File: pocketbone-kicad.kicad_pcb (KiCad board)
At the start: 2 copper layers, 55 x 35 mm, 64 parts, among them P1 USB_OTG, P2 USB_OTG, P3 CONN_01X10, P4 CONN_02X02, SW1 SW_PUSH_SMALL_H, SW2 SW_PUSH_SMALL_H, U1 SN74LVC1G07, U2 OSD3358, U3 24LC32AT-I/OT, U4 TPS2051C, Y2 24MHz

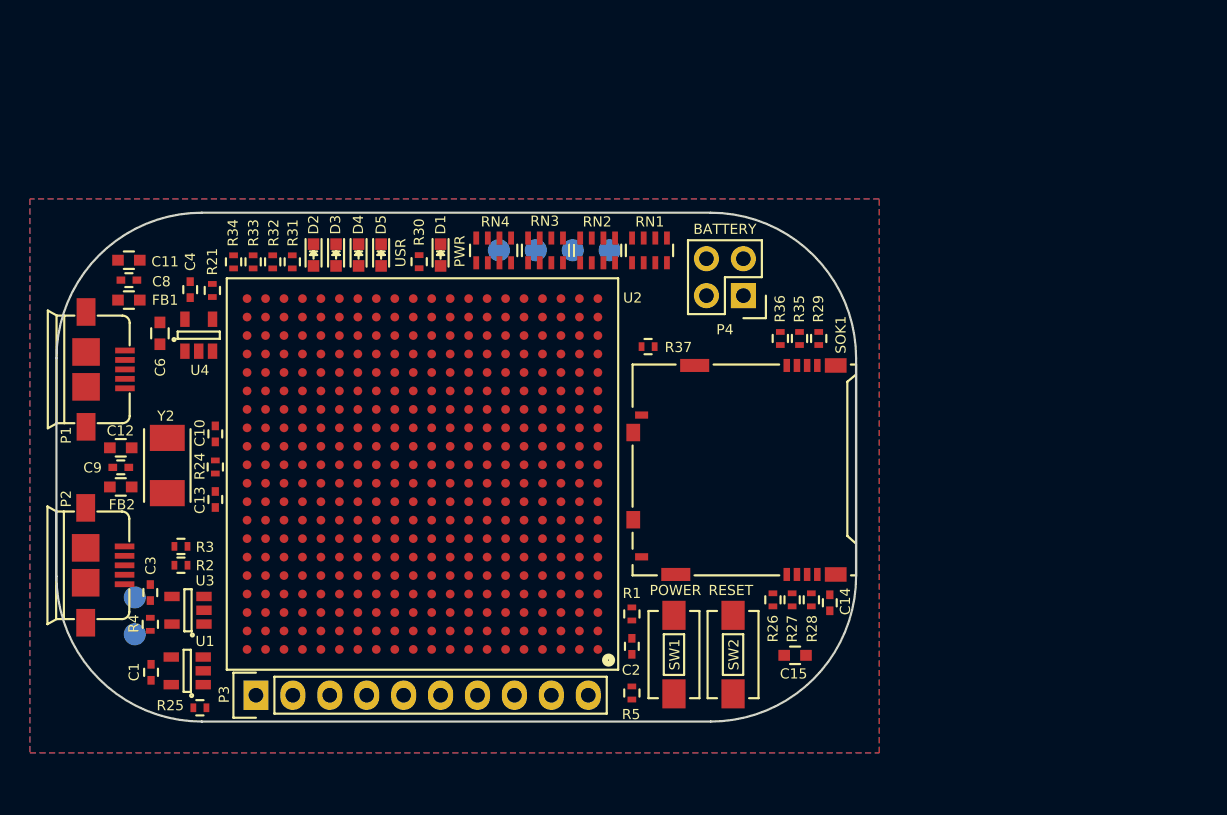
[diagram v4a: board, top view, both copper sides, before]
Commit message: Routing complete
Battery header updated in schmatic.
Plots and pictures updated.
Ready for design review.

Signed-off-by: Michael Welling <mwelling@ieee.org>
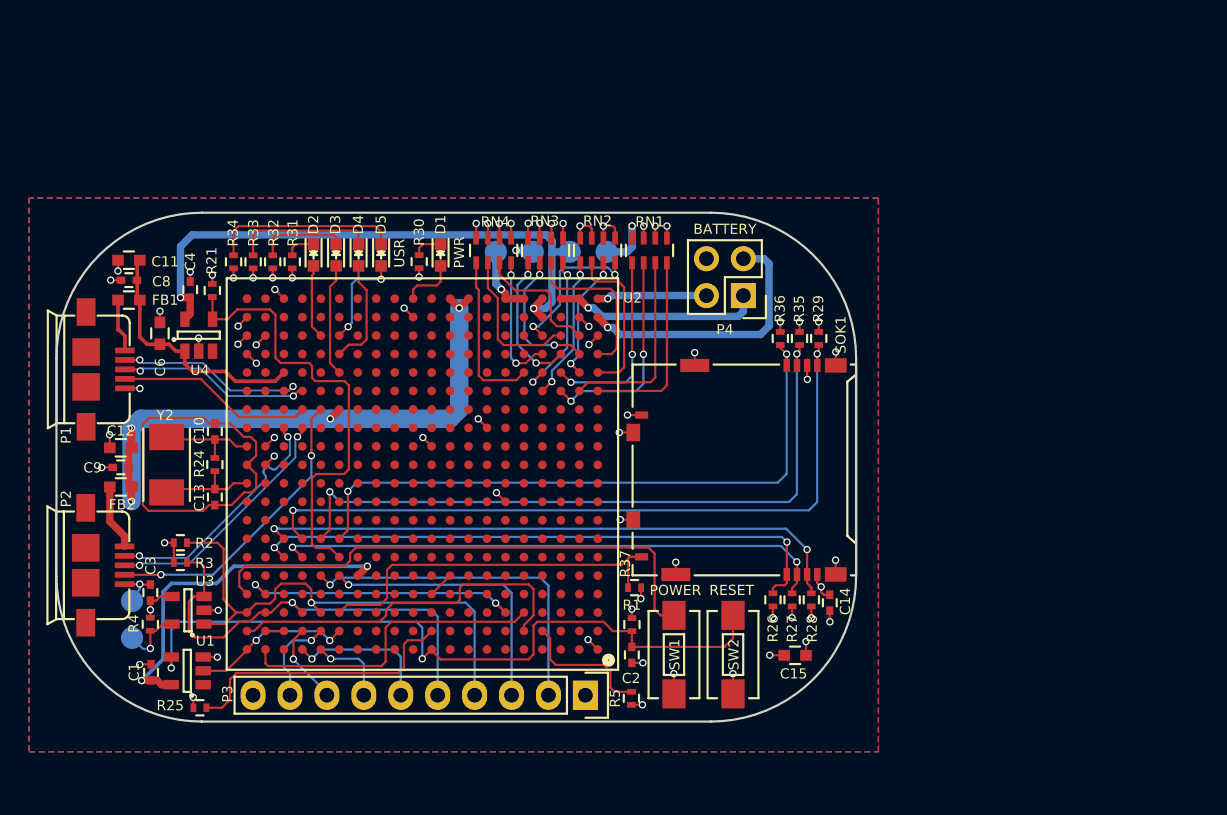
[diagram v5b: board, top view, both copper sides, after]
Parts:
- moved P3 22.7 mm to (142.3, 128.1), turned to 180 degrees
- moved R37 16.6 mm to (145.7, 120.7)
- moved G*** 1.79 mm to (113.1, 112.2)
- moved R2 1.55 mm to (114.5, 117.6)
- moved R3 1.11 mm to (114.5, 119.0)
- moved R1 0.73 mm to (145.5, 123.3)
- moved C2 0.59 mm to (145.5, 125.3)
- moved R5 0.37 mm to (145.5, 128.3)
- moved TP2 0.31 mm to (111.2, 124.2)
- moved TP3 0.31 mm to (111.2, 121.6)
- moved TP5 0.24 mm to (141.3, 97.6)
- moved TP6 0.24 mm to (143.8, 97.6)
- moved TP1 0.24 mm to (136.2, 97.6)
- moved TP4 0.24 mm to (138.7, 97.6)
- moved C13 0.17 mm to (116.9, 114.5)
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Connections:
- net Net-(P4-Pad3) renamed BAT_SENSE
- P4 pad 1: Net-(P4-Pad1) -> VBAT
- P4 pad 2: Net-(P4-Pad2) -> TS
- P4 pad 4: Net-(P4-Pad4) -> GND
- U2 pad W1: Net-(P4-Pad1) -> TS
- U2 pad Y2: Net-(P4-Pad2) -> VBAT
- U2 pad Y3: Net-(P4-Pad4) -> VBAT
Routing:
- net GND: track 0.00 -> 55.8 mm, vias 0 -> 57
- net Net-(C2-Pad1): track 0.00 -> 50.6 mm, vias 0 -> 2
- net MMC0_CLK: track 0.00 -> 50.2 mm, vias 0 -> 2
- net MMC0_DAT0: track 0.00 -> 47.2 mm, vias 0 -> 2
- net MMC0_DAT1: track 0.00 -> 44.0 mm, vias 0 -> 2
- net USB0_VBUS: track 0.00 -> 43.0 mm, vias 0 -> 4
- net MMC0_CMD: track 0.00 -> 41.3 mm, vias 0 -> 2
- net MMC0_DAT2: track 0.00 -> 40.9 mm, vias 0 -> 2
- net SYS_5V: track 0.00 -> 40.6 mm, vias 0 -> 2
- net MMC0_DAT3: track 0.00 -> 38.4 mm, vias 0 -> 2
- net Net-(SW1-Pad2): track 0.00 -> 36.8 mm
- net I2C0_SCL: track 0.00 -> 35.6 mm, vias 0 -> 1
- net I2C0_SDA: track 0.00 -> 31.7 mm, vias 0 -> 1
- net USB1_DRVVBUS: track 0.00 -> 30.9 mm
- net VDD_RTC: track 0.00 -> 27.0 mm, vias 0 -> 2
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- added copper zone on In1.Cu, net +3V3
- added copper zone on F.Cu, net GND
- added copper zone on In2.Cu, net GND
- removed copper zone on F.Cu, net +3V3
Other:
- copper layers 2 -> 4
- rule trace_min: 0.1524 -> 0.127
- board text added: "BS"
- board text added: "TS"
- board text added: "VBAT"

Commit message: Last minute tweaks
This version is posted to OSHpark site for anyone to order.
Order at your own risk.

Signed-off-by: Michael Welling <mwelling@ieee.org>
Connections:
- P1 pad 6: Net-(P1-Pad6) -> GND
- P1 pad 7: (no net) -> GND
- P1 pad 8: (no net) -> GND
- P1 pad 9: (no net) -> GND
- P2 pad 6: Net-(P2-Pad6) -> GND
- P2 pad 7: (no net) -> GND
- P2 pad 8: (no net) -> GND
- P2 pad 9: (no net) -> GND
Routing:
- net GND: track 55.8 -> 66.3 mm, vias 57 -> 65
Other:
- board text added: "PocketBone KiCAD Rev. 0 2017"

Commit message: Add OSHPark logo to the PCB and tweak the silk
OSHPark sponsoring the first proto run. \o/

https://oshpark.com/shared_projects/b7F6qftP

Signed-off-by: Michael Welling <mwelling@ieee.org>
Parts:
- added G***: LOGO, libs:oshpark, B.Cu at (135.6, 111.8)
- moved G*** 0.51 mm to (112.9, 111.8)
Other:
- board text added: "m_w"

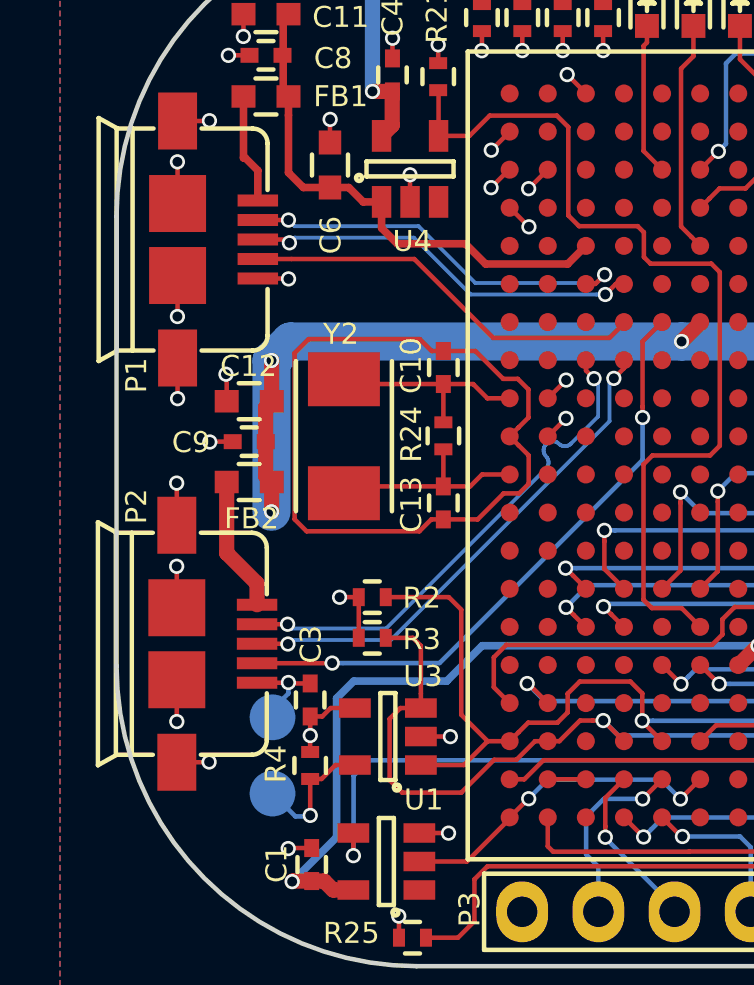
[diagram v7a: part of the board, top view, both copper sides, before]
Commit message: Updated Footprint and Schematic Librarys
The Paths of the USB and SOT Footprints pointed to local Directorys on
your HDD instead of the Project Folder
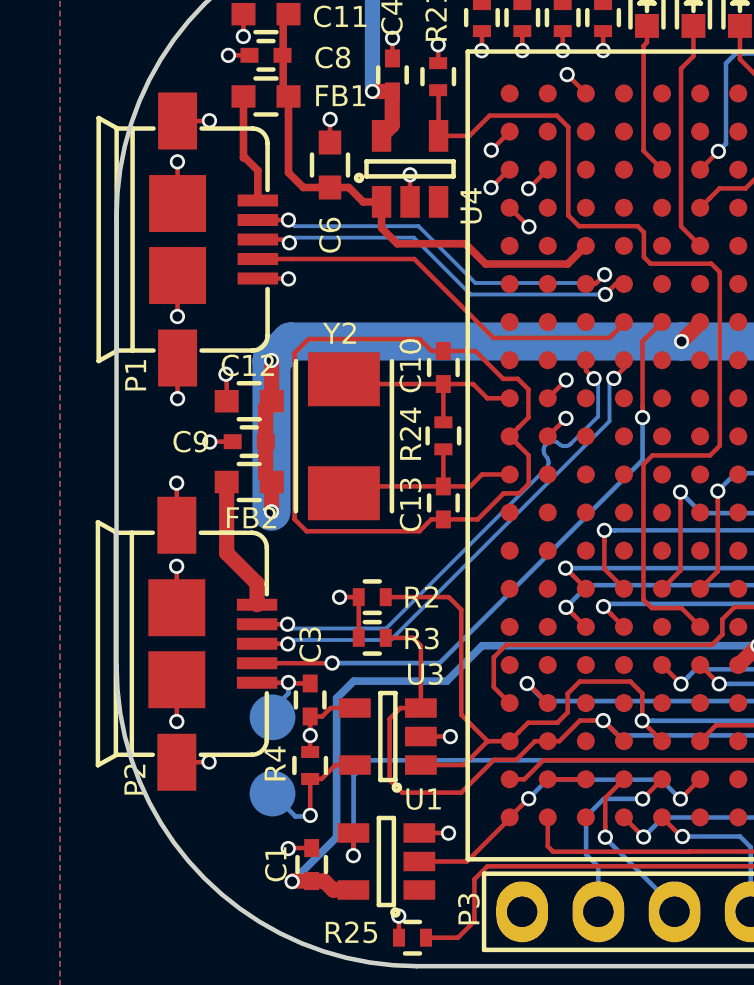
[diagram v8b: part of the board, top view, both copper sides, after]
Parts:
- P1, P2: footprint Sensors:USB_MICRO_B_ST-USB-001E -> pocketbone-kicad:USB_MICRO_B_ST-USB-001E
- U1, U3, U4: footprint SOT-23-5 -> pocketbone-kicad:SOT-23-5
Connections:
- P1 pad 7: GND -> (no net)
- P1 pad 8: GND -> (no net)
- P1 pad 9: GND -> (no net)
- P2 pad 7: GND -> (no net)
- P2 pad 8: GND -> (no net)
- P2 pad 9: GND -> (no net)
- U1 pad 1: Net-(U1-Pad1) -> (no net)
- U2 pad A11: Net-(U2-PadA11) -> (no net)
- U2 pad A12: Net-(U2-PadA12) -> (no net)
- U2 pad A13: Net-(U2-PadA13) -> (no net)
- U2 pad A14: Net-(U2-PadA14) -> (no net)
- U2 pad A15: Net-(U2-PadA15) -> (no net)
- U2 pad A18: Net-(U2-PadA18) -> (no net)
- U2 pad A2: Net-(U2-PadA2) -> (no net)
- U2 pad A3: Net-(U2-PadA3) -> (no net)
- U2 pad A4: Net-(U2-PadA4) -> (no net)
- U2 pad A5: Net-(U2-PadA5) -> (no net)
- U2 pad A6: Net-(U2-PadA6) -> (no net)
- U2 pad A7: Net-(U2-PadA7) -> (no net)
- U2 pad A8: Net-(U2-PadA8) -> (no net)
- U2 pad A9: Net-(U2-PadA9) -> (no net)
- U2 pad B1: Net-(U2-PadB1) -> (no net)
- U2 pad B11: Net-(U2-PadB11) -> (no net)
- U2 pad B12: Net-(U2-PadB12) -> (no net)
- U2 pad B13: Net-(U2-PadB13) -> (no net)
- U2 pad B14: Net-(U2-PadB14) -> (no net)
- U2 pad B2: Net-(U2-PadB2) -> (no net)
- U2 pad B3: Net-(U2-PadB3) -> (no net)
- U2 pad B6: Net-(U2-PadB6) -> (no net)
- U2 pad B7: Net-(U2-PadB7) -> (no net)
- U2 pad B8: Net-(U2-PadB8) -> (no net)
- U2 pad B9: Net-(U2-PadB9) -> (no net)
- U2 pad C1: Net-(U2-PadC1) -> (no net)
- U2 pad C10: Net-(U2-PadC10) -> (no net)
- U2 pad C11: Net-(U2-PadC11) -> (no net)
- U2 pad C12: Net-(U2-PadC12) -> (no net)
- U2 pad C13: Net-(U2-PadC13) -> (no net)
- U2 pad C14: Net-(U2-PadC14) -> (no net)
- U2 pad C18: Net-(U2-PadC18) -> (no net)
- U2 pad C2: Net-(U2-PadC2) -> (no net)
- U2 pad C3: Net-(U2-PadC3) -> (no net)
- U2 pad C4: Net-(U2-PadC4) -> (no net)
- U2 pad C7: Net-(U2-PadC7) -> (no net)
- U2 pad C8: Net-(U2-PadC8) -> (no net)
- U2 pad C9: Net-(U2-PadC9) -> (no net)
- U2 pad D1: Net-(U2-PadD1) -> (no net)
- U2 pad D11: Net-(U2-PadD11) -> (no net)
- U2 pad D12: Net-(U2-PadD12) -> (no net)
- U2 pad D13: Net-(U2-PadD13) -> (no net)
- U2 pad D14: Net-(U2-PadD14) -> (no net)
- U2 pad D15: Net-(U2-PadD15) -> (no net)
- U2 pad D16: Net-(U2-PadD16) -> (no net)
- U2 pad D17: Net-(U2-PadD17) -> (no net)
- U2 pad D18: Net-(U2-PadD18) -> (no net)
- U2 pad D2: Net-(U2-PadD2) -> (no net)
- U2 pad D3: Net-(U2-PadD3) -> (no net)
- U2 pad D4: Net-(U2-PadD4) -> (no net)
- U2 pad D5: Net-(U2-PadD5) -> (no net)
- U2 pad D6: Net-(U2-PadD6) -> (no net)
- U2 pad D7: Net-(U2-PadD7) -> (no net)
- U2 pad D8: Net-(U2-PadD8) -> (no net)
- U2 pad D9: Net-(U2-PadD9) -> (no net)
- U2 pad E1: Net-(U2-PadE1) -> (no net)
- U2 pad E10: Net-(U2-PadE10) -> (no net)
- U2 pad E11: Net-(U2-PadE11) -> (no net)
- U2 pad E12: Net-(U2-PadE12) -> (no net)
- U2 pad E13: Net-(U2-PadE13) -> (no net)
- U2 pad E17: Net-(U2-PadE17) -> (no net)
- U2 pad E18: Net-(U2-PadE18) -> (no net)
- U2 pad E19: Net-(U2-PadE19) -> (no net)
- U2 pad E2: Net-(U2-PadE2) -> (no net)
- U2 pad E20: Net-(U2-PadE20) -> (no net)
- U2 pad E3: Net-(U2-PadE3) -> (no net)
- U2 pad E4: Net-(U2-PadE4) -> (no net)
- U2 pad E5: Net-(U2-PadE5) -> (no net)
- U2 pad E6: Net-(U2-PadE6) -> (no net)
- U2 pad E7: Net-(U2-PadE7) -> (no net)
- U2 pad E8: Net-(U2-PadE8) -> (no net)
- U2 pad F1: Net-(U2-PadF1) -> (no net)
- U2 pad F10: Net-(U2-PadF10) -> (no net)
- U2 pad F11: Net-(U2-PadF11) -> (no net)
- U2 pad F12: Net-(U2-PadF12) -> (no net)
- U2 pad F13: Net-(U2-PadF13) -> (no net)
- U2 pad F14: Net-(U2-PadF14) -> (no net)
- U2 pad F16: Net-(U2-PadF16) -> (no net)
- U2 pad F19: Net-(U2-PadF19) -> (no net)
- U2 pad F2: Net-(U2-PadF2) -> (no net)
- U2 pad F20: Net-(U2-PadF20) -> (no net)
- U2 pad F3: Net-(U2-PadF3) -> (no net)
- U2 pad F4: Net-(U2-PadF4) -> (no net)
- U2 pad F5: Net-(U2-PadF5) -> (no net)
- U2 pad F6: Net-(U2-PadF6) -> (no net)
- U2 pad F7: Net-(U2-PadF7) -> (no net)
- U2 pad F8: Net-(U2-PadF8) -> (no net)
- U2 pad F9: Net-(U2-PadF9) -> (no net)
- U2 pad G1: Net-(U2-PadG1) -> (no net)
- U2 pad G10: Net-(U2-PadG10) -> (no net)
- U2 pad G11: Net-(U2-PadG11) -> (no net)
- U2 pad G12: Net-(U2-PadG12) -> (no net)
- U2 pad G13: Net-(U2-PadG13) -> (no net)
- U2 pad G14: Net-(U2-PadG14) -> (no net)
- U2 pad G19: Net-(U2-PadG19) -> (no net)
- U2 pad G2: Net-(U2-PadG2) -> (no net)
- U2 pad G20: Net-(U2-PadG20) -> (no net)
- U2 pad G3: Net-(U2-PadG3) -> (no net)
- U2 pad G4: Net-(U2-PadG4) -> (no net)
- U2 pad G5: Net-(U2-PadG5) -> (no net)
- U2 pad G6: Net-(U2-PadG6) -> (no net)
- U2 pad G7: Net-(U2-PadG7) -> (no net)
- U2 pad G8: Net-(U2-PadG8) -> (no net)
- U2 pad G9: Net-(U2-PadG9) -> (no net)
- U2 pad H1: Net-(U2-PadH1) -> (no net)
- U2 pad H10: Net-(U2-PadH10) -> (no net)
- U2 pad H11: Net-(U2-PadH11) -> (no net)
- U2 pad H12: Net-(U2-PadH12) -> (no net)
- U2 pad H13: Net-(U2-PadH13) -> (no net)
- U2 pad H14: Net-(U2-PadH14) -> (no net)
- U2 pad H15: Net-(U2-PadH15) -> (no net)
- U2 pad H16: Net-(U2-PadH16) -> (no net)
- U2 pad H17: Net-(U2-PadH17) -> (no net)
- U2 pad H18: Net-(U2-PadH18) -> (no net)
- U2 pad H19: Net-(U2-PadH19) -> (no net)
- U2 pad H2: Net-(U2-PadH2) -> (no net)
- U2 pad H20: Net-(U2-PadH20) -> (no net)
- U2 pad H3: Net-(U2-PadH3) -> (no net)
- U2 pad H4: Net-(U2-PadH4) -> (no net)
- U2 pad H5: Net-(U2-PadH5) -> (no net)
- U2 pad H6: Net-(U2-PadH6) -> (no net)
- U2 pad H7: Net-(U2-PadH7) -> (no net)
- U2 pad H8: Net-(U2-PadH8) -> (no net)
- U2 pad H9: Net-(U2-PadH9) -> (no net)
- U2 pad J1: Net-(U2-PadJ1) -> (no net)
- U2 pad J10: Net-(U2-PadJ10) -> (no net)
- U2 pad J11: Net-(U2-PadJ11) -> (no net)
- U2 pad J12: Net-(U2-PadJ12) -> (no net)
- U2 pad J13: Net-(U2-PadJ13) -> (no net)
- U2 pad J14: Net-(U2-PadJ14) -> (no net)
- U2 pad J15: Net-(U2-PadJ15) -> (no net)
- U2 pad J16: Net-(U2-PadJ16) -> (no net)
- U2 pad J17: Net-(U2-PadJ17) -> (no net)
- U2 pad J18: Net-(U2-PadJ18) -> (no net)
- U2 pad J19: Net-(U2-PadJ19) -> (no net)
- U2 pad J2: Net-(U2-PadJ2) -> (no net)
- U2 pad J20: Net-(U2-PadJ20) -> (no net)
- U2 pad J3: Net-(U2-PadJ3) -> (no net)
- U2 pad J4: Net-(U2-PadJ4) -> (no net)
- U2 pad J5: Net-(U2-PadJ5) -> (no net)
- U2 pad J7: Net-(U2-PadJ7) -> (no net)
- U2 pad J8: Net-(U2-PadJ8) -> (no net)
- U2 pad J9: Net-(U2-PadJ9) -> (no net)
- U2 pad K1: Net-(U2-PadK1) -> (no net)
- U2 pad K10: Net-(U2-PadK10) -> (no net)
- U2 pad K11: Net-(U2-PadK11) -> (no net)
- U2 pad K12: Net-(U2-PadK12) -> (no net)
- U2 pad K13: Net-(U2-PadK13) -> (no net)
- U2 pad K14: Net-(U2-PadK14) -> (no net)
- U2 pad K15: Net-(U2-PadK15) -> (no net)
- U2 pad K16: Net-(U2-PadK16) -> (no net)
- U2 pad K17: Net-(U2-PadK17) -> (no net)
- U2 pad K18: Net-(U2-PadK18) -> (no net)
- U2 pad K19: Net-(U2-PadK19) -> (no net)
- U2 pad K2: Net-(U2-PadK2) -> (no net)
- U2 pad K3: Net-(U2-PadK3) -> (no net)
- U2 pad K4: Net-(U2-PadK4) -> (no net)
- U2 pad K5: Net-(U2-PadK5) -> (no net)
- U2 pad K6: Net-(U2-PadK6) -> (no net)
- U2 pad K7: Net-(U2-PadK7) -> (no net)
- U2 pad K8: Net-(U2-PadK8) -> (no net)
- U2 pad K9: Net-(U2-PadK9) -> (no net)
- U2 pad L1: Net-(U2-PadL1) -> (no net)
- U2 pad L10: Net-(U2-PadL10) -> (no net)
- U2 pad L11: Net-(U2-PadL11) -> (no net)
- U2 pad L12: Net-(U2-PadL12) -> (no net)
- U2 pad L13: Net-(U2-PadL13) -> (no net)
- U2 pad L14: Net-(U2-PadL14) -> (no net)
- U2 pad L15: Net-(U2-PadL15) -> (no net)
- U2 pad L16: Net-(U2-PadL16) -> (no net)
- U2 pad L17: Net-(U2-PadL17) -> (no net)
- U2 pad L18: Net-(U2-PadL18) -> (no net)
- U2 pad L2: Net-(U2-PadL2) -> (no net)
- U2 pad L3: Net-(U2-PadL3) -> (no net)
- U2 pad L4: Net-(U2-PadL4) -> (no net)
- U2 pad L5: Net-(U2-PadL5) -> (no net)
- U2 pad L6: Net-(U2-PadL6) -> (no net)
- U2 pad L7: Net-(U2-PadL7) -> (no net)
- U2 pad L8: Net-(U2-PadL8) -> (no net)
- U2 pad L9: Net-(U2-PadL9) -> (no net)
- U2 pad M1: Net-(U2-PadM1) -> (no net)
- U2 pad M11: Net-(U2-PadM11) -> (no net)
- U2 pad M12: Net-(U2-PadM12) -> (no net)
- U2 pad M13: Net-(U2-PadM13) -> (no net)
- U2 pad M14: Net-(U2-PadM14) -> (no net)
- U2 pad M15: Net-(U2-PadM15) -> (no net)
- U2 pad M16: Net-(U2-PadM16) -> (no net)
- U2 pad M17: Net-(U2-PadM17) -> (no net)
- U2 pad M18: Net-(U2-PadM18) -> (no net)
- U2 pad M2: Net-(U2-PadM2) -> (no net)
- U2 pad M3: Net-(U2-PadM3) -> (no net)
- U2 pad M4: Net-(U2-PadM4) -> (no net)
- U2 pad M5: Net-(U2-PadM5) -> (no net)
- U2 pad M6: Net-(U2-PadM6) -> (no net)
- U2 pad M7: Net-(U2-PadM7) -> (no net)
- U2 pad M8: Net-(U2-PadM8) -> (no net)
- U2 pad M9: Net-(U2-PadM9) -> (no net)
- U2 pad N1: Net-(U2-PadN1) -> (no net)
- U2 pad N10: Net-(U2-PadN10) -> (no net)
- U2 pad N11: Net-(U2-PadN11) -> (no net)
- U2 pad N12: Net-(U2-PadN12) -> (no net)
- U2 pad N13: Net-(U2-PadN13) -> (no net)
- U2 pad N14: Net-(U2-PadN14) -> (no net)
- U2 pad N15: Net-(U2-PadN15) -> (no net)
- U2 pad N16: Net-(U2-PadN16) -> (no net)
- U2 pad N19: Net-(U2-PadN19) -> (no net)
- U2 pad N2: Net-(U2-PadN2) -> (no net)
- U2 pad N20: Net-(U2-PadN20) -> (no net)
- U2 pad N3: Net-(U2-PadN3) -> (no net)
- U2 pad N4: Net-(U2-PadN4) -> (no net)
- U2 pad N5: Net-(U2-PadN5) -> (no net)
- U2 pad N6: Net-(U2-PadN6) -> (no net)
- U2 pad N8: Net-(U2-PadN8) -> (no net)
- U2 pad N9: Net-(U2-PadN9) -> (no net)
- U2 pad P1: Net-(U2-PadP1) -> (no net)
- U2 pad P10: Net-(U2-PadP10) -> (no net)
- U2 pad P11: Net-(U2-PadP11) -> (no net)
- U2 pad P12: Net-(U2-PadP12) -> (no net)
- U2 pad P13: Net-(U2-PadP13) -> (no net)
- U2 pad P14: Net-(U2-PadP14) -> (no net)
- U2 pad P18: Net-(U2-PadP18) -> (no net)
- U2 pad P19: Net-(U2-PadP19) -> (no net)
- U2 pad P2: Net-(U2-PadP2) -> (no net)
- U2 pad P20: Net-(U2-PadP20) -> (no net)
- U2 pad P3: Net-(U2-PadP3) -> (no net)
- U2 pad P4: Net-(U2-PadP4) -> (no net)
- U2 pad P5: Net-(U2-PadP5) -> (no net)
- U2 pad P6: Net-(U2-PadP6) -> (no net)
- U2 pad P7: Net-(U2-PadP7) -> (no net)
- U2 pad P8: Net-(U2-PadP8) -> (no net)
- U2 pad P9: Net-(U2-PadP9) -> (no net)
- U2 pad R10: Net-(U2-PadR10) -> (no net)
- U2 pad R11: Net-(U2-PadR11) -> (no net)
- U2 pad R12: Net-(U2-PadR12) -> (no net)
- U2 pad R13: Net-(U2-PadR13) -> (no net)
- U2 pad R14: Net-(U2-PadR14) -> (no net)
- U2 pad R15: Net-(U2-PadR15) -> (no net)
- U2 pad R16: Net-(U2-PadR16) -> (no net)
- U2 pad R19: Net-(U2-PadR19) -> (no net)
- U2 pad R20: Net-(U2-PadR20) -> (no net)
- U2 pad R5: Net-(U2-PadR5) -> (no net)
- U2 pad R6: Net-(U2-PadR6) -> (no net)
- U2 pad R7: Net-(U2-PadR7) -> (no net)
- U2 pad R8: Net-(U2-PadR8) -> (no net)
- U2 pad R9: Net-(U2-PadR9) -> (no net)
- U2 pad T10: Net-(U2-PadT10) -> (no net)
- U2 pad T11: Net-(U2-PadT11) -> (no net)
- U2 pad T12: Net-(U2-PadT12) -> (no net)
- U2 pad T13: Net-(U2-PadT13) -> (no net)
- U2 pad T14: Net-(U2-PadT14) -> (no net)
- U2 pad T16: Net-(U2-PadT16) -> (no net)
- U2 pad T17: Net-(U2-PadT17) -> (no net)
- U2 pad T19: Net-(U2-PadT19) -> (no net)
- U2 pad T20: Net-(U2-PadT20) -> (no net)
- U2 pad T6: Net-(U2-PadT6) -> (no net)
- U2 pad T7: Net-(U2-PadT7) -> (no net)
- U2 pad T8: Net-(U2-PadT8) -> (no net)
- U2 pad T9: Net-(U2-PadT9) -> (no net)
- U2 pad U10: Net-(U2-PadU10) -> (no net)
- U2 pad U11: Net-(U2-PadU11) -> (no net)
- U2 pad U12: Net-(U2-PadU12) -> (no net)
- U2 pad U13: Net-(U2-PadU13) -> (no net)
- U2 pad U14: Net-(U2-PadU14) -> (no net)
- U2 pad U16: Net-(U2-PadU16) -> (no net)
- U2 pad U17: Net-(U2-PadU17) -> (no net)
- U2 pad U18: Net-(U2-PadU18) -> (no net)
- U2 pad U19: Net-(U2-PadU19) -> (no net)
- U2 pad U5: Net-(U2-PadU5) -> (no net)
- U2 pad U6: Net-(U2-PadU6) -> (no net)
- U2 pad U7: Net-(U2-PadU7) -> (no net)
- U2 pad U8: Net-(U2-PadU8) -> (no net)
- U2 pad U9: Net-(U2-PadU9) -> (no net)
- U2 pad V10: Net-(U2-PadV10) -> (no net)
- U2 pad V11: Net-(U2-PadV11) -> (no net)
- U2 pad V12: Net-(U2-PadV12) -> (no net)
- U2 pad V13: Net-(U2-PadV13) -> (no net)
- U2 pad V14: Net-(U2-PadV14) -> (no net)
- U2 pad V17: Net-(U2-PadV17) -> (no net)
- U2 pad V18: Net-(U2-PadV18) -> (no net)
- U2 pad V5: Net-(U2-PadV5) -> (no net)
- U2 pad V6: Net-(U2-PadV6) -> (no net)
- U2 pad V7: Net-(U2-PadV7) -> (no net)
- U2 pad V8: Net-(U2-PadV8) -> (no net)
- U2 pad V9: Net-(U2-PadV9) -> (no net)
- U2 pad W10: Net-(U2-PadW10) -> (no net)
- U2 pad W12: Net-(U2-PadW12) -> (no net)
- U2 pad W13: Net-(U2-PadW13) -> (no net)
- U2 pad W14: Net-(U2-PadW14) -> (no net)
- U2 pad W15: Net-(U2-PadW15) -> (no net)
- U2 pad W16: Net-(U2-PadW16) -> (no net)
- U2 pad W17: Net-(U2-PadW17) -> (no net)
- U2 pad W18: Net-(U2-PadW18) -> (no net)
- U2 pad W19: Net-(U2-PadW19) -> (no net)
- U2 pad W3: Net-(U2-PadW3) -> (no net)
- U2 pad W5: Net-(U2-PadW5) -> (no net)
- U2 pad W6: Net-(U2-PadW6) -> (no net)
- U2 pad W7: Net-(U2-PadW7) -> (no net)
- U2 pad W8: Net-(U2-PadW8) -> (no net)
- U2 pad W9: Net-(U2-PadW9) -> (no net)
- U2 pad Y10: Net-(U2-PadY10) -> (no net)
- U2 pad Y12: Net-(U2-PadY12) -> (no net)
- U2 pad Y13: Net-(U2-PadY13) -> (no net)
- U2 pad Y14: Net-(U2-PadY14) -> (no net)
- U2 pad Y15: Net-(U2-PadY15) -> (no net)
- U2 pad Y16: Net-(U2-PadY16) -> (no net)
- U2 pad Y17: Net-(U2-PadY17) -> (no net)
- U2 pad Y19: Net-(U2-PadY19) -> (no net)
- U2 pad Y20: Net-(U2-PadY20) -> (no net)
- U2 pad Y7: Net-(U2-PadY7) -> (no net)
- U4 pad 3: Net-(U4-Pad3) -> (no net)
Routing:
- net (no net): track 0.00 -> 8.01 mm, vias 0 -> 6
- net GND: track 66.3 -> 58.2 mm, vias 65 -> 59
